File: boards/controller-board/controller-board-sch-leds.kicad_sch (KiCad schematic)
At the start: 60 parts, among them U10 MP2410A, U11 MP2410A, U6 MP2410A, U7 MP2410A, U8 MP2410A, U9 MP2410A

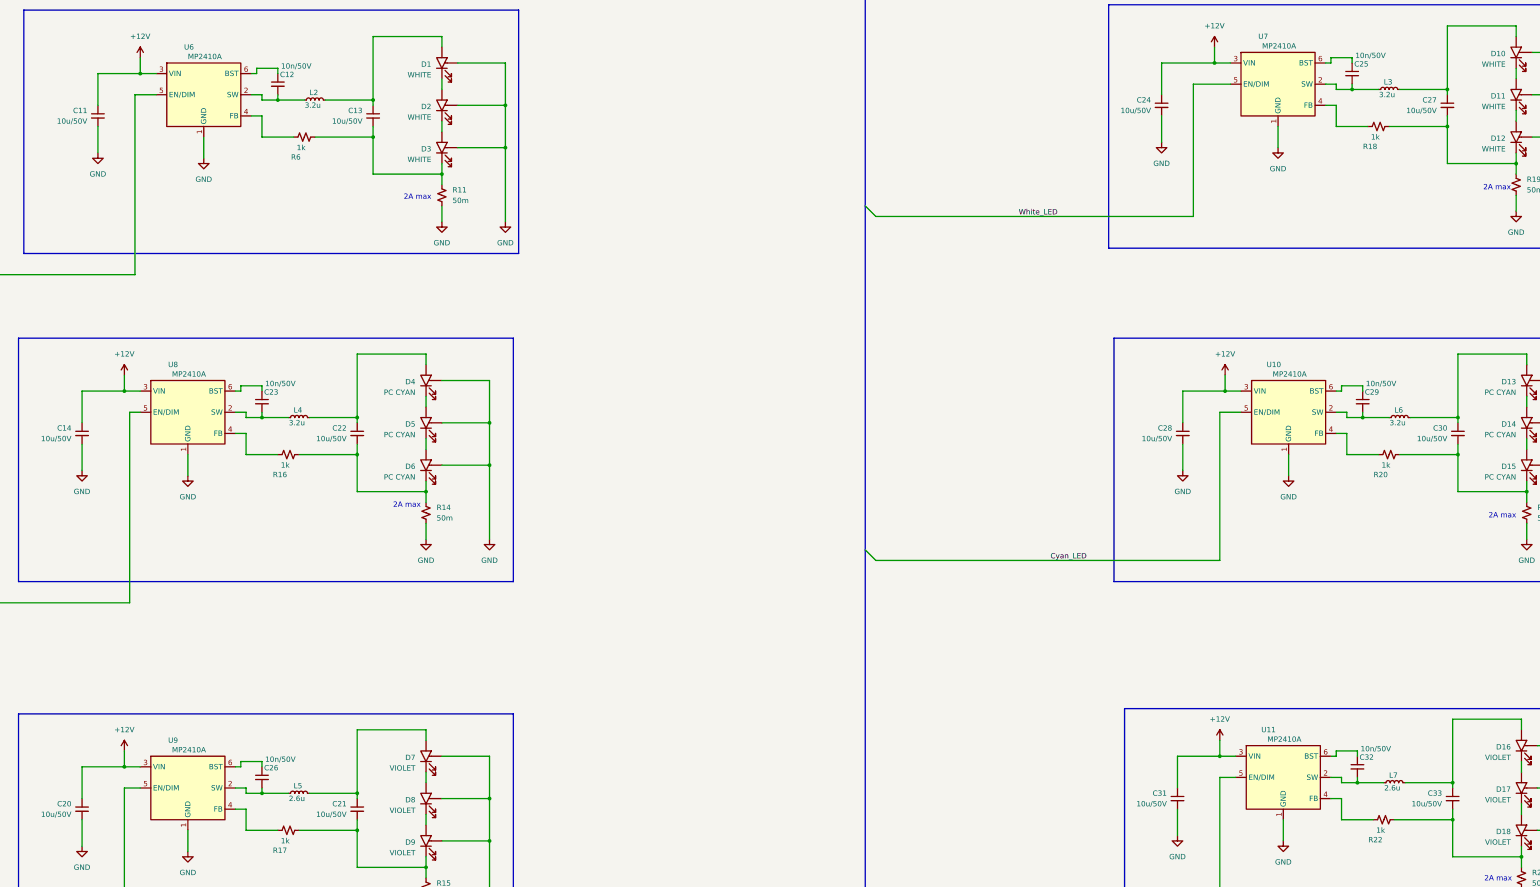
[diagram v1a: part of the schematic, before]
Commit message: Clean up library links, fix ERC errors, dix DRC errors, add more 3D models, and add makefile and readme.
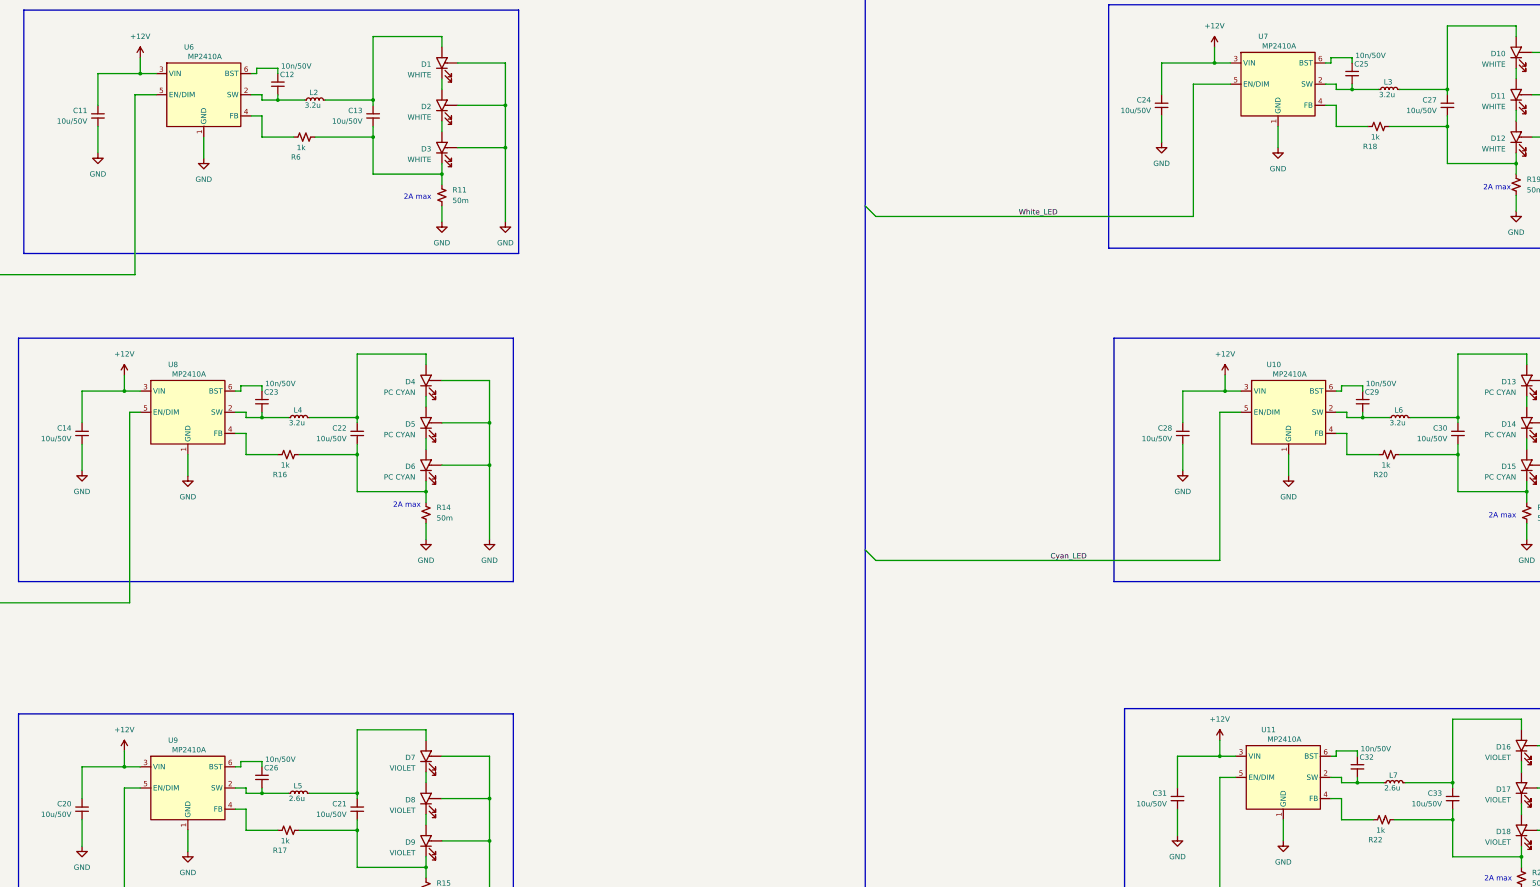
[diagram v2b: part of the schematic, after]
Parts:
- C11, C12, C13, C14, C20, C21, C22, C23, C24, C25, C26, C27, C28, C29, C30, C31, C32, C33, D1, D10, D11, D12, D13, D14, D15, D16, D17, D18, D2, D3, D4, D5, D6, D7, D8, D9, L2, L3, L4, L5, L6, L7, R11, R14, R15, R16, R17, R18, R19, R20, R21, R22, R23, R6, U10, U11, U6, U7, U8, U9: DIS (none) -> DigiKey; Distributor DigiKey -> (none)
